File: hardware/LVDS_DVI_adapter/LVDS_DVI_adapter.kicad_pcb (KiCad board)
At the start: 2 copper layers, 20.9 x 19.8 mm, 18 parts, among them J1 DF12NB(3.0)-30DS-0.5V(51), J2 HDMI_A, U1 TXS0102DCU

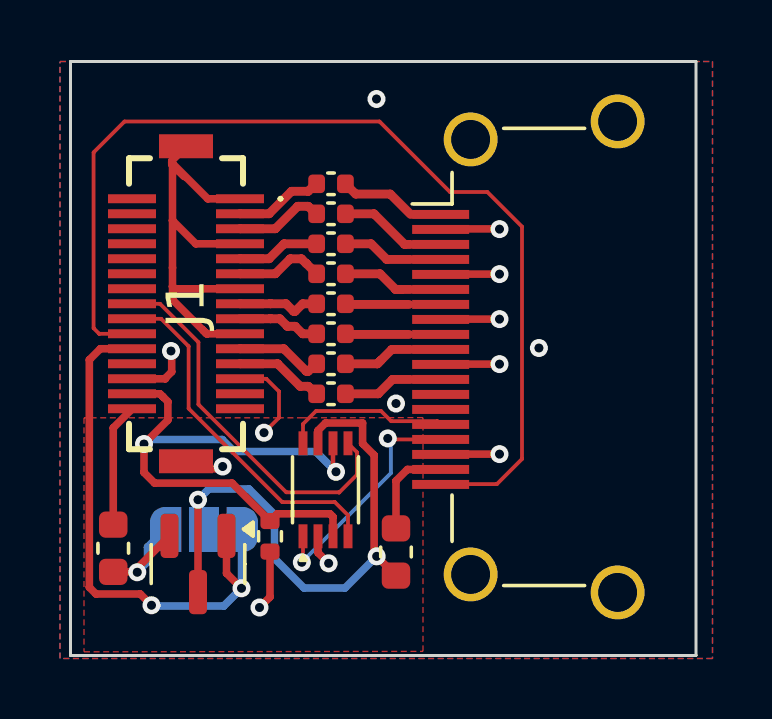
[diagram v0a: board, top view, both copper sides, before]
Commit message: Add 3.3V to 5V pump as DVI power (HE9009M6R) and general fixes
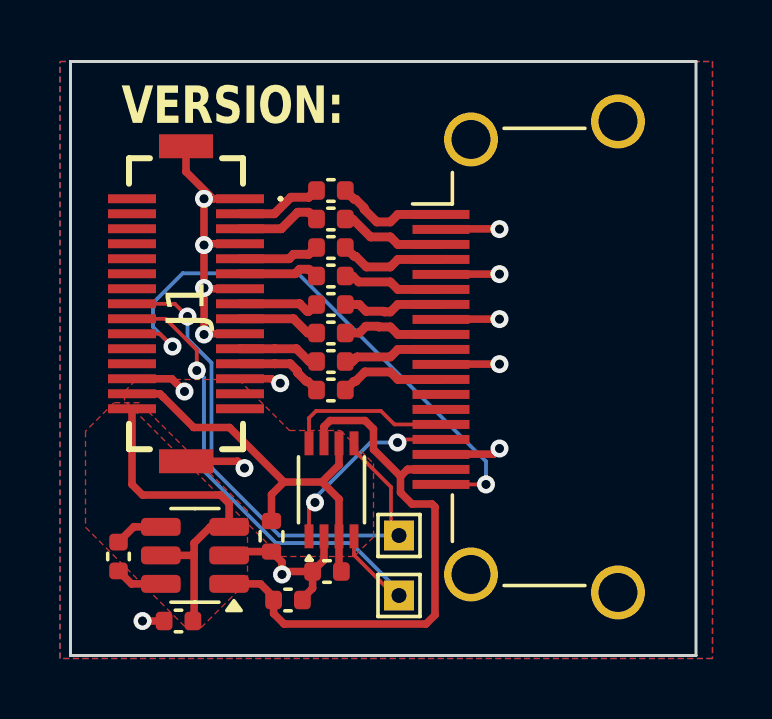
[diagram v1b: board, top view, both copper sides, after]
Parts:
- removed D3: BAT54C, Package_TO_SOT_SMD:SOT-23
- removed F1: Fuse_Small, Fuse:Fuse_0603_1608Metric
- removed FB1: 100 ohm @ 100 MHz, Inductor_SMD:L_0603_1608Metric
- removed JP1: SolderJumper_3_Open, Jumper:SolderJumper-3_P1.3mm_Open_RoundedPad1.0x1.5mm
- added C10: 2.2uF, Capacitor_SMD:C_0402_1005Metric, F.Cu at (129.9, 129.7)
- added C11: 2.2uF, Capacitor_SMD:C_0402_1005Metric, F.Cu at (127.9, 127.5)
- added C12: 0.1uF, Capacitor_SMD:C_0402_1005Metric, F.Cu at (134.8, 128.0)
- added C9: 2.2uF, Capacitor_SMD:C_0402_1005Metric, F.Cu at (133.6, 128.9)
- added TP2: TP_SCL, TestPoint:TestPoint_THTPad_1.0x1.0mm_Drill0.5mm, F.Cu at (137.2, 128.8)
- added TP3: TP_SDA, TestPoint:TestPoint_THTPad_1.0x1.0mm_Drill0.5mm, F.Cu at (137.2, 126.8)
- added U2: HE9009M6R, Package_TO_SOT_SMD:SOT-23-6, F.Cu at (130.4, 127.5)
- moved G*** 16.4 mm to (130.2, 113.1)
- moved G*** 12.8 mm to (142.4, 120.4)
- moved C1 0.22 mm to (135.0, 115.3)
- moved U1 0.20 mm to (135.0, 125.3)
- moved C2 0.17 mm to (135.0, 116.2)
- moved C8 0.13 mm to (135.0, 122.0)
- moved C3 0.12 mm to (135.0, 117.2)
- moved C7 0.08 mm to (135.0, 121.0)
- moved C4 0.07 mm to (135.0, 118.2)
- moved R1 0.05 mm to (133.0, 126.8)
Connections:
- J1 pad 22: 5V0 -> unconnected-(J1-21-Pad22)
- J1 pad 30: Net-(J1-29) -> +3V3
- J2 pad 18: CONN_5V0 -> PDVI_VCC
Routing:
- net 5V0: track 18.7 -> 0.00 mm, vias 2 -> 0
- net HPD: track 34.2 -> 19.6 mm, vias 0 -> 2
- net +3V3: track 4.27 -> 11.9 mm, vias 1 -> 0
- net VIO: track 19.6 -> 13.8 mm, vias 2 -> 0
- net SCL: track 11.8 -> 17.5 mm, vias 0 -> 1
- net SDA: track 12.7 -> 18.1 mm, vias 0 -> 1
- net Net-(J1-29): track 4.12 -> 0.00 mm
- net CONN_5V0: track 3.23 -> 0.00 mm
- net GND: track 35.7 -> 33.2 mm, vias 13 -> 14
- net SCL_SHIFTED: track 8.13 -> 6.36 mm
- net Net-(U2-CN): track 0.00 -> 1.62 mm
- net Net-(U2-CP): track 0.00 -> 1.59 mm
- net PDVI_VCC: track 19.4 -> 20.3 mm, vias 2 -> 0
- net DVI_1_N: track 3.89 -> 3.36 mm
- added copper zone on F.Cu, net +3V3
- added copper zone on F.Cu, net VIO
- removed copper zone on F.Cu, net PDVI_VCC
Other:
- board text added: "Passive DVI adapter v0.1"
- board text added: "VERSION:"
- board text removed: "Passive DVI adapter"

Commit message: improve return plane for better signal integrity in LVDS DVI adapter
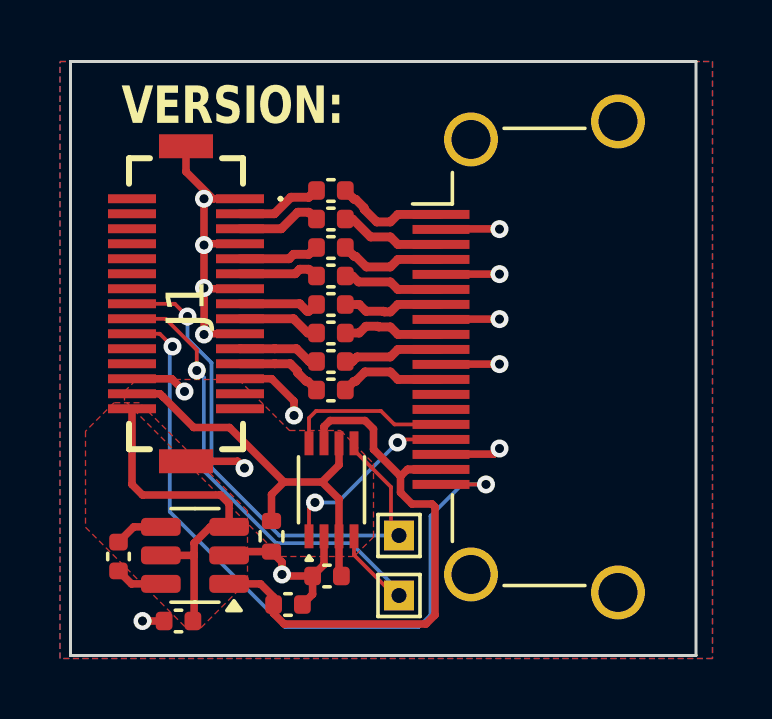
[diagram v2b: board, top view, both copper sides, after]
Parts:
- moved C12 0.15 mm to (134.8, 128.2)
- moved C9 0.15 mm to (133.6, 129.1)
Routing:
- net HPD: track 19.6 -> 24.6 mm
- net GND: track 33.2 -> 34.4 mm
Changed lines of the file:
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@@
 		(tags "SOT TO_SOT_SMD")
 		(property "Reference" "U2"
-			(at -0.051256 -0.0875 -180)
+			(at -0.051256 -0.0875 180)
 			(layer "B.SilkS")
 			(effects
@@
 	(footprint "Capacitor_SMD:C_0402_1005Metric"
 		(layer "F.Cu")
-		(at 134.85 128)
+		(at 134.85 128.15)
 		(descr "Capacitor SMD 0402 (1005 Metric), square (rectangular) end terminal, IPC_7351 nominal, (Body size source: IPC-SM-782 page 76, https://www.pcb-3d.com/wordpress/wp-content/uploads/ipc-sm-782a_amendment_1_and_2.pdf), generated with kicad-footprint-generator")
 		(tags "capacitor")
@@
 		)
 		(property "Value" "0.1uF"
-			(at 0 1.16 360)
+			(at 0 1.16 0)
 			(layer "F.Fab")
 			(effects
@@
 		)
 		(fp_text user "${REFERENCE}"
-			(at 0 0 360)
+			(at 0 0 0)
 			(layer "F.Fab")
 			(effects
@@
 		(tags "capacitor")
 		(property "Reference" "C11"
-			(at -0.1 -0.15 270)
+			(at -0.1 -0.15 -90)
 			(layer "B.SilkS")
 			(effects
@@
 		)
 		(property "Value" "2.2uF"
-			(at 0 1.16 270)
+			(at 0 1.16 -90)
 			(layer "F.Fab")
 			(effects
@@
 		)
 		(fp_text user "${REFERENCE}"
-			(at 0 0 270)
+			(at 0 0 -90)
 			(layer "F.Fab")
 			(effects
@@
 	(footprint "Capacitor_SMD:C_0402_1005Metric"
 		(layer "F.Cu")
-		(at 133.55 128.95)
+		(at 133.55 129.1)
 		(descr "Capacitor SMD 0402 (1005 Metric), square (rectangular) end terminal, IPC_7351 nominal, (Body size source: IPC-SM-782 page 76, https://www.pcb-3d.com/wordpress/wp-content/uploads/ipc-sm-782a_amendment_1_and_2.pdf), generated with kicad-footprint-generator")
 		(tags "capacitor")
@@
 	)
 	(segment
-		(start 133.35 128.1)
-		(end 133.45 128)
-		(width 0.254)
-		(layer "F.Cu")
-		(net 1)
-	)
-	(segment
-		(start 133.1525 121.7235)
-		(end 133.004 121.575)
+		(start 134.37 128.76)
+		(end 134.37 128.15)
 		(width 0.254)
 		(layer "F.Cu")
@@
 	)
 	(segment
-		(start 134.37 128.56)
-		(end 134.37 128)
-		(width 0.254)
-		(layer "F.Cu")
-		(net 1)
-	)
-	(segment
 		(start 133 127.337)
 		(end 133.35 127.687)
@@
 	)
 	(segment
-		(start 133.004 121.575)
-		(end 131.95 121.575)
+		(start 130.75 117.117897)
+		(end 130.75 118.55)
 		(width 0.254)
 		(layer "F.Cu")
@@
 	(segment
 		(start 130.75 117.117897)
-		(end 130.75 118.55)
+		(end 130.792897 117.075)
 		(width 0.254)
 		(layer "F.Cu")
@@
 	)
 	(segment
-		(start 134.03 128.9)
-		(end 134.37 128.56)
+		(start 130.75 115.575)
+		(end 131.05 115.575)
 		(width 0.254)
 		(layer "F.Cu")
@@
 	)
 	(segment
-		(start 130.75 117.117897)
-		(end 130.792897 117.075)
+		(start 130.15 114.675)
+		(end 130.15 113.825)
 		(width 0.254)
 		(layer "F.Cu")
@@
 	)
 	(segment
-		(start 133.292656 121.7235)
-		(end 133.1525 121.7235)
+		(start 133.75 122.8)
+		(end 133.75 122.321)
 		(width 0.254)
 		(layer "F.Cu")
@@
 	)
 	(segment
-		(start 130.75 115.575)
-		(end 131.05 115.575)
+		(start 131.871 124.325)
+		(end 130.15 124.325)
 		(width 0.254)
 		(layer "F.Cu")
@@
 	)
 	(segment
-		(start 130.15 114.675)
-		(end 130.15 113.825)
+		(start 133.004 121.575)
+		(end 131.95 121.575)
 		(width 0.254)
 		(layer "F.Cu")
@@
 	)
 	(segment
-		(start 131.871 124.325)
-		(end 130.15 124.325)
+		(start 134.75 127.77)
+		(end 134.75 126.827)
 		(width 0.254)
 		(layer "F.Cu")
@@
 	)
 	(segment
-		(start 134.75 127.62)
-		(end 134.75 126.827)
+		(start 133.35 128.1)
+		(end 133.4 128.15)
 		(width 0.254)
 		(layer "F.Cu")
@@
 	)
 	(segment
-		(start 134.37 128)
-		(end 134.75 127.62)
-		(width 0.254)
-		(layer "F.Cu")
-		(net 1)
-	)
-	(segment
 		(start 129.677 121.577)
 		(end 128.36 121.577)
@@
 	)
 	(segment
-		(start 138.65 121.08715)
-		(end 140.6 121.08715)
+		(start 134.03 129.1)
+		(end 134.37 128.76)
 		(width 0.254)
 		(layer "F.Cu")
@@
 	)
 	(segment
-		(start 133.45 128)
-		(end 134.37 128)
+		(start 138.65 121.08715)
+		(end 140.6 121.08715)
 		(width 0.254)
 		(layer "F.Cu")
@@
 	)
 	(segment
+		(start 133.4 128.15)
+		(end 134.22 128.15)
+		(width 0.254)
+		(layer "F.Cu")
+		(net 1)
+	)
+	(segment
 		(start 130.775 120.075)
 		(end 130.75 120.1)
@@
 	)
 	(segment
+		(start 133.75 122.321)
+		(end 133.004 121.575)
+		(width 0.254)
+		(layer "F.Cu")
+		(net 1)
+	)
+	(segment
 		(start 131.711744 127.337)
 		(end 133 127.337)
@@
 	)
 	(segment
+		(start 134.37 128.15)
+		(end 134.75 127.77)
+		(width 0.254)
+		(layer "F.Cu")
+		(net 1)
+	)
+	(segment
 		(start 131.586244 127.4625)
 		(end 131.711744 127.337)
@@
 	)
 	(via
-		(at 133.292656 121.7235)
+		(at 133.75 122.8)
 		(size 0.6)
 		(drill 0.3)
@@
 	)
 	(segment
-		(start 140.15 124.330822)
-		(end 133.878678 118.0595)
+		(start 129.6095 126.0095)
+		(end 129.6095 120.5905)
 		(width 0.127)
 		(layer "B.Cu")
@@
 	)
 	(segment
-		(start 140.15 125.098)
-		(end 140.15 124.330822)
+		(start 137.9 129.85)
+		(end 133.45 129.85)
+		(width 0.127)
+		(layer "B.Cu")
+		(net 23)
+	)
+	(segment
+		(start 133.45 129.85)
+		(end 129.6095 126.0095)
 		(width 0.127)
 		(layer "B.Cu")
@@
 	)
 	(segment
-		(start 130.0405 118.0595)
-		(end 129.05 119.05)
+		(start 139.352 125.098)
+		(end 138.3 126.15)
 		(width 0.127)
 		(layer "B.Cu")
@@
 	)
 	(segment
-		(start 129.05 119.85)
+		(start 129.6095 120.5905)
 		(end 129.7 120.5)
 		(width 0.127)
@@
 	)
 	(segment
-		(start 133.878678 118.0595)
-		(end 130.0405 118.0595)
+		(start 138.3 126.15)
+		(end 138.3 129.45)
 		(width 0.127)
 		(layer "B.Cu")
@@
 	)
 	(segment
-		(start 129.05 119.05)
-		(end 129.05 119.85)
+		(start 140.15 125.098)
+		(end 139.352 125.098)
+		(width 0.127)
+		(layer "B.Cu")
+		(net 23)
+	)
+	(segment
+		(start 138.3 129.45)
+		(end 137.9 129.85)
 		(width 0.127)
 		(layer "B.Cu")
@@
 	)
 	(segment
-		(start 135.33 128)
-		(end 135.25 127.92)
-		(width 0.254)
-		(layer "F.Cu")
-		(net 25)
-	)
-	(segment
-		(start 135.25 125.584)
-		(end 134.683 125.017)
+		(start 129.284 122.077)
+		(end 129.379 122.172)
 		(width 0.254)
 		(layer "F.Cu")
@@
 	)
 	(segment
-		(start 129.284 122.077)
-		(end 129.379 122.172)
+		(start 135.33 128.15)
+		(end 135.25 128.07)
 		(width 0.254)
 		(layer "F.Cu")
@@
 	)
 	(segment
-		(start 128.36 122.077)
-		(end 129.284 122.077)
+		(start 135.25 125.584)
+		(end 134.683 125.017)
 		(width 0.254)
 		(layer "F.Cu")
@@
 	)
 	(segment
-		(start 129.382357 122.175357)
-		(end 130.407 123.2)
+		(start 128.36 122.077)
+		(end 129.284 122.077)
 		(width 0.254)
 		(layer "F.Cu")
@@
 	)
 	(segment
-		(start 135.25 127.92)
-		(end 135.25 125.584)
+		(start 129.382357 122.175357)
+		(end 130.407 123.2)
 		(width 0.254)
 		(layer "F.Cu")
@@
 	)
 	(segment
+		(start 135.25 128.07)
+		(end 135.25 125.584)
+		(width 0.254)
+		(layer "F.Cu")
+		(net 25)
+	)
+	(segment
 		(start 131.6 123.2)
 		(end 133.417 125.017)
@@
 	)
 	(segment
-		(start 134.45 125.55)
-		(end 136.3 123.7)
-		(width 0.127)
-		(layer "B.Cu")
-		(net 27)
-	)
-	(segment
-		(start 136.3 123.7)
+		(start 135.2 125.7)
 		(end 137.2 123.7)
 		(width 0.127)
@@
 	(segment
 		(start 134.45 125.7)
-		(end 134.45 125.55)
+		(end 135.2 125.7)
 		(width 0.127)
 		(layer "B.Cu")
@@
 			)
 		)
+	)
+	(zone
+		(net 0)
+		(net_name "")
+		(layer "B.Cu")
+		(hatch edge 0.5)
+		(connect_pads
+			(clearance 0)
+		)
+		(min_thickness 0.25)
+		(filled_areas_thickness no)
+		(keepout
+			(tracks not_allowed)
+			(vias not_allowed)
+			(pads allowed)
+			(copperpour allowed)
+			(footprints not_allowed)
+		)
+		(fill
+			(thermal_gap 0.5)
+			(thermal_bridge_width 0.5)
+		)
+		(polygon
+			(pts
+				(xy 131.55 115.8) (xy 132.55 114.8) (xy 138.7 114.8) (xy 139.8 115.9) (xy 139.8 121.45) (xy 138.85 122.4)
+				(xy 132.45 122.4) (xy 131.55 121.5)
+			)
+		)

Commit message: review and update manufacturing constraints (via size, etc.)
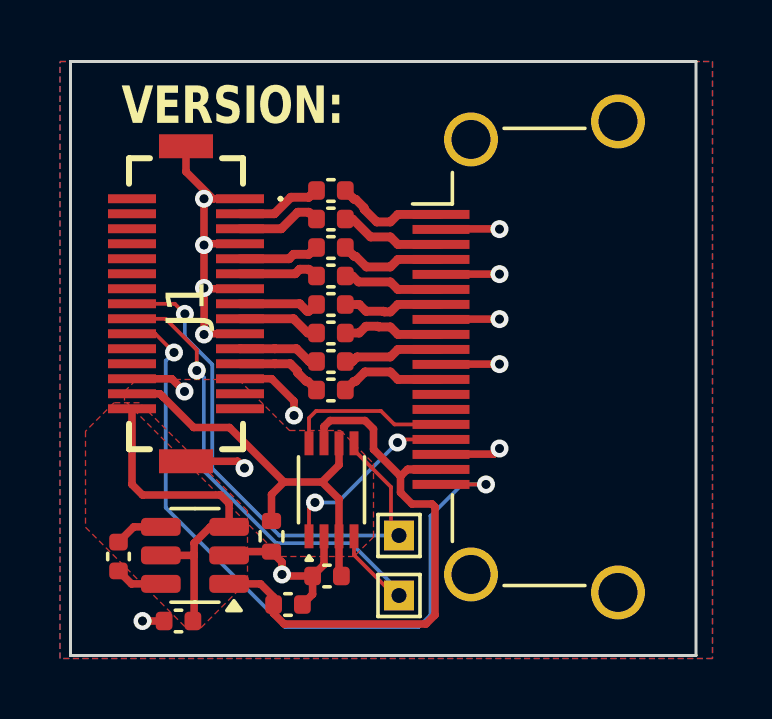
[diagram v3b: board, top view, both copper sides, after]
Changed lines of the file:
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@@
-	)
-	(segment
-		(start 129.777 119.077)
-		(end 130.2 119.5)
-		(width 0.127)
-		(layer "F.Cu")
-		(net 2)
-	)
-	(segment
-		(start 129.720664 119.077)
-		(end 128.36 119.077)
-		(width 0.127)
-		(layer "F.Cu")
-		(net 2)
 	)
 	(segment
@@
 	)
 	(segment
+		(start 129.777 119.077)
+		(end 128.36 119.077)
+		(width 0.127)
+		(layer "F.Cu")
+		(net 2)
+	)
+	(segment
 		(start 136.9825 126.6825)
 		(end 137.1 126.8)
@@
 	)
 	(segment
-		(start 129.720664 119.077)
+		(start 130.1125 119.4125)
 		(end 129.777 119.077)
 		(width 0.127)
@@
 	)
 	(via
-		(at 130.2 119.5)
+		(at 130.1125 119.4125)
 		(size 0.6)
 		(drill 0.3)
@@
 	)
 	(segment
-		(start 130.2 119.5)
-		(end 130.2 120.243672)
-		(width 0.127)
-		(layer "B.Cu")
-		(net 2)
-	)
-	(segment
-		(start 131 121.043672)
-		(end 131 124.54079)
+		(start 130.1125 120.1875)
+		(end 131.025 121.1)
+		(width 0.127)
+		(layer "B.Cu")
+		(net 2)
+	)
+	(segment
+		(start 131.025 124.56579)
+		(end 133.25921 126.8)
+		(width 0.127)
+		(layer "B.Cu")
+		(net 2)
+	)
+	(segment
+		(start 130.1125 119.4125)
+		(end 130.1125 120.1875)
+		(width 0.127)
+		(layer "B.Cu")
+		(net 2)
+	)
+	(segment
+		(start 131.025 121.1)
+		(end 131.025 124.56579)
 		(width 0.127)
 		(layer "B.Cu")
@@
 		(start 133.25921 126.8)
 		(end 137.1 126.8)
-		(width 0.127)
-		(layer "B.Cu")
-		(net 2)
-	)
-	(segment
-		(start 130.2 120.243672)
-		(end 131 121.043672)
-		(width 0.127)
-		(layer "B.Cu")
-		(net 2)
-	)
-	(segment
-		(start 131 124.54079)
-		(end 133.25921 126.8)
 		(width 0.127)
 		(layer "B.Cu")
@@
 	)
 	(segment
+		(start 130.746 121.5365)
+		(end 130.746 124.646)
+		(width 0.127)
+		(layer "B.Cu")
+		(net 3)
+	)
+	(segment
+		(start 137.1 128.5)
+		(end 137.1 128.8)
+		(width 0.127)
+		(layer "B.Cu")
+		(net 3)
+	)
+	(segment
+		(start 133.154 127.054)
+		(end 135.654 127.054)
+		(width 0.127)
+		(layer "B.Cu")
+		(net 3)
+	)
+	(segment
 		(start 130.746 124.646)
 		(end 133.154 127.054)
@@
 	)
 	(segment
-		(start 133.154 127.054)
-		(end 135.654 127.054)
-		(width 0.127)
-		(layer "B.Cu")
-		(net 3)
-	)
-	(segment
-		(start 130.746 121.5365)
-		(end 130.746 124.646)
-		(width 0.127)
-		(layer "B.Cu")
-		(net 3)
-	)
-	(segment
-		(start 137.1 128.5)
-		(end 137.1 128.8)
-		(width 0.127)
-		(layer "B.Cu")
-		(net 3)
-	)
-	(segment
 		(start 135.702751 121)
 		(end 135.854801 120.84795)
@@
 	)
 	(segment
-		(start 129.275 120.075)
+		(start 129.75 120.7)
+		(end 129.125 120.075)
+		(width 0.127)
+		(layer "F.Cu")
+		(net 23)
+	)
+	(segment
+		(start 129.125 120.075)
 		(end 128.35 120.075)
 		(width 0.127)
@@
 		(net 23)
 	)
-	(segment
-		(start 129.7 120.5)
-		(end 129.275 120.075)
-		(width 0.127)
-		(layer "F.Cu")
-		(net 23)
-	)
 	(via
-		(at 129.7 120.5)
+		(at 129.75 120.7)
 		(size 0.6)
 		(drill 0.3)
@@
 	)
 	(segment
-		(start 129.6095 126.0095)
-		(end 129.6095 120.5905)
+		(start 129.75 120.7)
+		(end 129.475 120.975)
+		(width 0.127)
+		(layer "B.Cu")
+		(net 23)
+	)
+	(segment
+		(start 138.3 126.15)
+		(end 139.352 125.098)
+		(width 0.127)
+		(layer "B.Cu")
+		(net 23)
+	)
+	(segment
+		(start 138.3 129.45)
+		(end 138.3 126.15)
+		(width 0.127)
+		(layer "B.Cu")
+		(net 23)
+	)
+	(segment
+		(start 133.45 129.85)
+		(end 137.9 129.85)
+		(width 0.127)
+		(layer "B.Cu")
+		(net 23)
+	)
+	(segment
+		(start 129.475 120.975)
+		(end 129.475 125.875)
 		(width 0.127)
 		(layer "B.Cu")
@@
 	(segment
 		(start 137.9 129.85)
+		(end 138.3 129.45)
+		(width 0.127)
+		(layer "B.Cu")
+		(net 23)
+	)
+	(segment
+		(start 139.352 125.098)
+		(end 140.15 125.098)
+		(width 0.127)
+		(layer "B.Cu")
+		(net 23)
+	)
+	(segment
+		(start 129.475 125.875)
 		(end 133.45 129.85)
 		(width 0.127)
 		(layer "B.Cu")
-		(net 23)
-	)
-	(segment
-		(start 133.45 129.85)
-		(end 129.6095 126.0095)
-		(width 0.127)
-		(layer "B.Cu")
-		(net 23)
-	)
-	(segment
-		(start 139.352 125.098)
-		(end 138.3 126.15)
-		(width 0.127)
-		(layer "B.Cu")
-		(net 23)
-	)
-	(segment
-		(start 129.6095 120.5905)
-		(end 129.7 120.5)
-		(width 0.127)
-		(layer "B.Cu")
-		(net 23)
-	)
-	(segment
-		(start 138.3 126.15)
-		(end 138.3 129.45)
-		(width 0.127)
-		(layer "B.Cu")
-		(net 23)
-	)
-	(segment
-		(start 140.15 125.098)
-		(end 139.352 125.098)
-		(width 0.127)
-		(layer "B.Cu")
-		(net 23)
-	)
-	(segment
-		(start 138.3 129.45)
-		(end 137.9 129.85)
-		(width 0.127)
-		(layer "B.Cu")
